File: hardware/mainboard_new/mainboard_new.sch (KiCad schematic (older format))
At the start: 11 parts, among them M1 LOGIC_LEVEL_CONVERTER, Q1 BS170

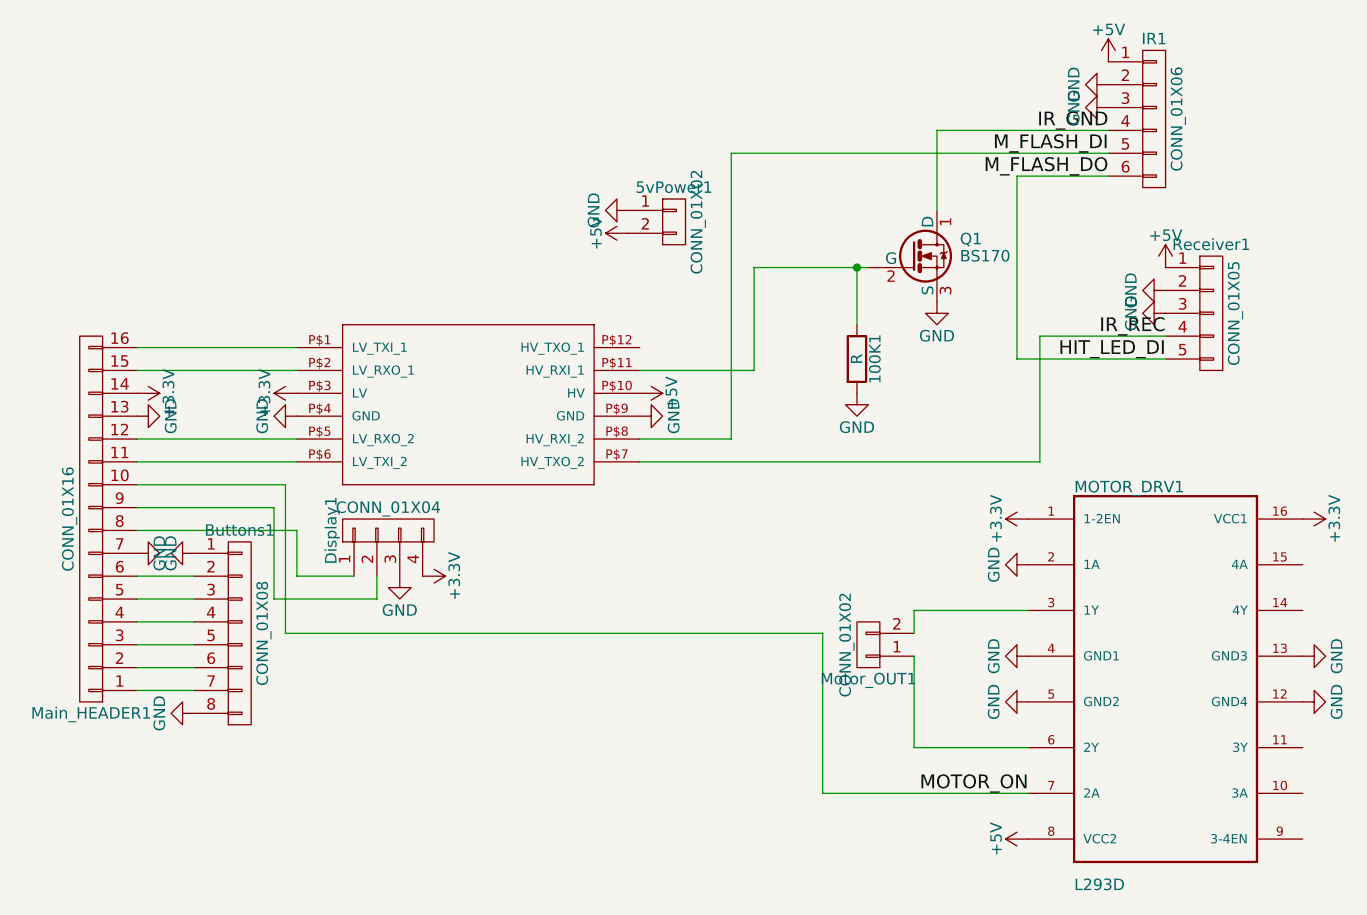
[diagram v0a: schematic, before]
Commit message: #9 JST Pins added
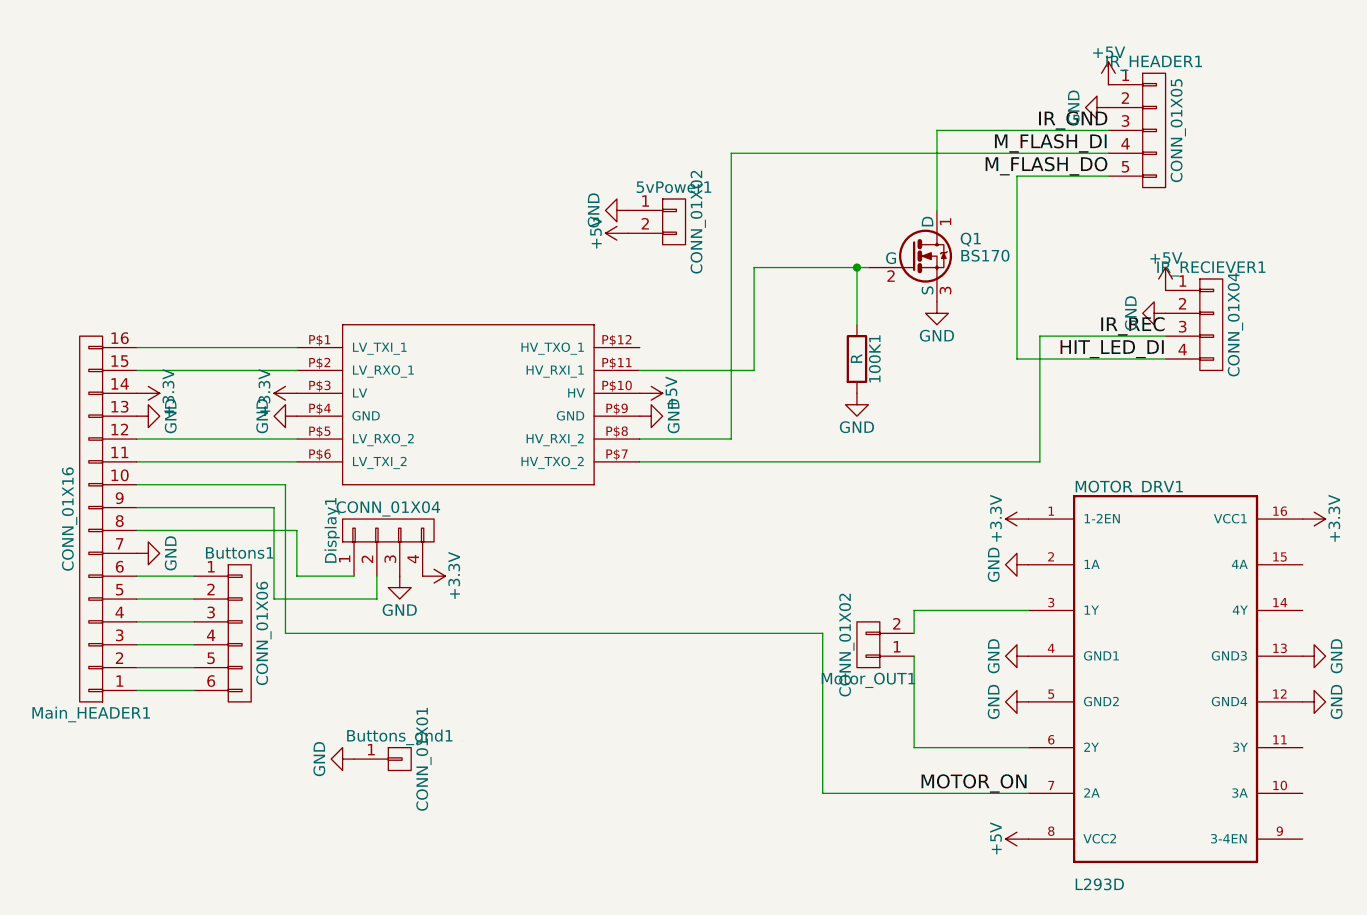
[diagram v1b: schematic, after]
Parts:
- removed Buttons1: CONN_01X08, Socket_Strips:Socket_Strip_Straight_1x08_Pitch2.54mm, symbol CONN_01X08
- removed IR1: CONN_01X06, Socket_Strips:Socket_Strip_Straight_1x06_Pitch2.54mm, symbol CONN_01X06
- removed Receiver1: CONN_01X05, Socket_Strips:Socket_Strip_Straight_1x05_Pitch2.54mm, symbol CONN_01X05
- added Buttons1: CONN_01X06, Connectors_JST:JST_EH_B06B-EH-A_06x2.50mm_Straight, symbol CONN_01X06
- added Buttons_gnd1: CONN_01X01, Socket_Strips:Socket_Strip_Straight_1x01_Pitch1.27mm, symbol CONN_01X01
- added IR_HEADER1: CONN_01X05, Connectors_JST:JST_EH_B05B-EH-A_05x2.50mm_Straight, symbol CONN_01X05
- added IR_RECIEVER1: CONN_01X04, Connectors_JST:JST_EH_B04B-EH-A_04x2.50mm_Straight, symbol CONN_01X04
- 5vPower1: footprint Socket_Strips:Socket_Strip_Straight_1x02_Pitch2.54mm -> Connectors_JST:JST_EH_B02B-EH-A_02x2.50mm_Straight
- Display1: footprint Socket_Strips:Socket_Strip_Straight_1x04_Pitch2.54mm -> Connectors_JST:JST_EH_B04B-EH-A_04x2.50mm_Straight
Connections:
- net +5V: now also IR_HEADER1.1 (P1), IR_RECIEVER1.1 (P1)
- net GND: now also Buttons_gnd1.1 (P1), IR_HEADER1.2 (P2), IR_RECIEVER1.2 (P2)
- net HIT_LED_DI: now also IR_HEADER1.5 (P5), IR_RECIEVER1.4 (P4)
- net IR_GND: now also IR_HEADER1.3 (P3)
- net IR_REC: now also IR_RECIEVER1.3 (P3)
- net M_FLASH_DI: now also IR_HEADER1.4 (P4)
- net at Main_HEADER1.1 (P1): now also Buttons1.6 (P6)
- net at Main_HEADER1.2 (P2): now also Buttons1.5 (P5)
- net at Main_HEADER1.3 (P3): now also Buttons1.4 (P4)
- net at Main_HEADER1.4 (P4): now also Buttons1.3 (P3)
- net at Main_HEADER1.5 (P5): now also Buttons1.2 (P2)
- net at Main_HEADER1.6 (P6): now also Buttons1.1 (P1)
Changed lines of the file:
@@
 F 0 "Display1" H 3300 3800 50  0000 C CNN
 F 1 "CONN_01X04" V 3400 3550 50  0000 C CNN
-F 2 "Socket_Strips:Socket_Strip_Straight_1x04_Pitch2.54mm" H 3300 3550 50  0001 C CNN
+F 2 "Connectors_JST:JST_EH_B04B-EH-A_04x2.50mm_Straight" H 3300 3550 50  0001 C CNN
 F 3 "" H 3300 3550 50  0001 C CNN
 	1    3300 3550
@@
 F 0 "5vPower1" H 4550 2350 50  0000 C CNN
 F 1 "CONN_01X02" V 4650 2200 50  0000 C CNN
-F 2 "Socket_Strips:Socket_Strip_Straight_1x02_Pitch2.54mm" H 4550 2200 50  0001 C CNN
+F 2 "Connectors_JST:JST_EH_B02B-EH-A_02x2.50mm_Straight" H 4550 2200 50  0001 C CNN
 F 3 "" H 4550 2200 50  0001 C CNN
 	1    4550 2200
@@
 $EndComp
 $Comp
-L GND #PWR018
-U 1 1 59666C99
-P 2450 4350
-F 0 "#PWR018" H 2450 4100 50  0001 C CNN
-F 1 "GND" H 2450 4200 50  0000 C CNN
-F 2 "" H 2450 4350 50  0001 C CNN
-F 3 "" H 2450 4350 50  0001 C CNN
-	1    2450 4350
-	0    1    1    0
-$EndComp
-$Comp
-L CONN_01X05 Receiver1
-U 1 1 59666DC7
-P 6900 2600
-F 0 "Receiver1" H 6900 2900 50  0000 C CNN
-F 1 "CONN_01X05" V 7000 2600 50  0000 C CNN
-F 2 "Socket_Strips:Socket_Strip_Straight_1x05_Pitch2.54mm" H 6900 2600 50  0001 C CNN
-F 3 "" H 6900 2600 50  0001 C CNN
-	1    6900 2600
-	1    0    0    -1
-$EndComp
-$Comp
-L +5V #PWR019
+L +5V #PWR017
 U 1 1 59666EE0
-P 6700 2400
-F 0 "#PWR019" H 6700 2250 50  0001 C CNN
-F 1 "+5V" H 6700 2540 50  0000 C CNN
-F 2 "" H 6700 2400 50  0001 C CNN
-F 3 "" H 6700 2400 50  0001 C CNN
-	1    6700 2400
-	1    0    0    -1
-$EndComp
-$Comp
-L GND #PWR020
-U 1 1 59666F02
 P 6700 2500
-F 0 "#PWR020" H 6700 2250 50  0001 C CNN
-F 1 "GND" H 6700 2350 50  0000 C CNN
+F 0 "#PWR017" H 6700 2350 50  0001 C CNN
+F 1 "+5V" H 6700 2640 50  0000 C CNN
 F 2 "" H 6700 2500 50  0001 C CNN
 F 3 "" H 6700 2500 50  0001 C CNN
 	1    6700 2500
-	0    1    1    0
-$EndComp
-$Comp
-L GND #PWR021
+	1    0    0    -1
+$EndComp
+$Comp
+L GND #PWR018
 U 1 1 59666F24
 P 6700 2600
-F 0 "#PWR021" H 6700 2350 50  0001 C CNN
+F 0 "#PWR018" H 6700 2350 50  0001 C CNN
 F 1 "GND" H 6700 2450 50  0000 C CNN
 F 2 "" H 6700 2600 50  0001 C CNN
@@
 $EndComp
 $Comp
-L CONN_01X06 IR1
-U 1 1 59667064
-P 6650 1750
-F 0 "IR1" H 6650 2100 50  0000 C CNN
-F 1 "CONN_01X06" V 6750 1750 50  0000 C CNN
-F 2 "Socket_Strips:Socket_Strip_Straight_1x06_Pitch2.54mm" H 6650 1750 50  0001 C CNN
-F 3 "" H 6650 1750 50  0001 C CNN
-	1    6650 1750
-	1    0    0    -1
-$EndComp
-$Comp
-L +5V #PWR022
+L +5V #PWR019
 U 1 1 596670F4
-P 6450 1500
-F 0 "#PWR022" H 6450 1350 50  0001 C CNN
-F 1 "+5V" H 6450 1640 50  0000 C CNN
-F 2 "" H 6450 1500 50  0001 C CNN
-F 3 "" H 6450 1500 50  0001 C CNN
-	1    6450 1500
-	1    0    0    -1
-$EndComp
-$Comp
-L GND #PWR023
-U 1 1 59667118
 P 6450 1600
-F 0 "#PWR023" H 6450 1350 50  0001 C CNN
-F 1 "GND" H 6450 1450 50  0000 C CNN
+F 0 "#PWR019" H 6450 1450 50  0001 C CNN
+F 1 "+5V" H 6450 1740 50  0000 C CNN
 F 2 "" H 6450 1600 50  0001 C CNN
 F 3 "" H 6450 1600 50  0001 C CNN
 	1    6450 1600
-	0    1    1    0
-$EndComp
-$Comp
-L GND #PWR024
+	1    0    0    -1
+$EndComp
+$Comp
+L GND #PWR020
 U 1 1 5966713C
 P 6450 1700
-F 0 "#PWR024" H 6450 1450 50  0001 C CNN
+F 0 "#PWR020" H 6450 1450 50  0001 C CNN
 F 1 "GND" H 6450 1550 50  0000 C CNN
 F 2 "" H 6450 1700 50  0001 C CNN
@@
 $EndComp
 $Comp
-L GND #PWR025
+L GND #PWR021
 U 1 1 59667252
 P 5350 2950
-F 0 "#PWR025" H 5350 2700 50  0001 C CNN
+F 0 "#PWR021" H 5350 2700 50  0001 C CNN
 F 1 "GND" H 5350 2800 50  0000 C CNN
 F 2 "" H 5350 2950 50  0001 C CNN
@@
 $EndComp
 $Comp
-L GND #PWR026
+L GND #PWR022
 U 1 1 5966727A
 P 5700 2550
-F 0 "#PWR026" H 5700 2300 50  0001 C CNN
+F 0 "#PWR022" H 5700 2300 50  0001 C CNN
 F 1 "GND" H 5700 2400 50  0000 C CNN
 F 2 "" H 5700 2550 50  0001 C CNN
@@
 	2800 3850 3250 3850
 $Comp
-L GND #PWR027
+L GND #PWR023
 U 1 1 59669886
 P 3350 3750
-F 0 "#PWR027" H 3350 3500 50  0001 C CNN
+F 0 "#PWR023" H 3350 3500 50  0001 C CNN
 F 1 "GND" H 3350 3600 50  0000 C CNN
 F 2 "" H 3350 3750 50  0001 C CNN
@@
 $EndComp
 $Comp
-L +3.3V #PWR028
+L +3.3V #PWR024
 U 1 1 596698AE
 P 3450 3750
-F 0 "#PWR028" H 3450 3600 50  0001 C CNN
+F 0 "#PWR024" H 3450 3600 50  0001 C CNN
 F 1 "+3.3V" H 3450 3890 50  0000 C CNN
 F 2 "" H 3450 3750 50  0001 C CNN
@@
 $EndComp
 $Comp
-L GND #PWR029
+L GND #PWR025
 U 1 1 59669E34
 P 4400 3050
-F 0 "#PWR029" H 4400 2800 50  0001 C CNN
+F 0 "#PWR025" H 4400 2800 50  0001 C CNN
 F 1 "GND" H 4400 2900 50  0000 C CNN
 F 2 "" H 4400 3050 50  0001 C CNN
@@
 Wire Wire Line
 	4900 2850 4900 2400
-$Comp
-L CONN_01X08 Buttons1
-U 1 1 59666B16
+Wire Wire Line
+	2200 3750 2450 3750
+Wire Wire Line
+	2200 3850 2450 3850
+Wire Wire Line
+	2200 3950 2450 3950
+Wire Wire Line
+	2200 4050 2450 4050
+Wire Wire Line
+	2200 4150 2450 4150
+Wire Wire Line
+	2200 4250 2450 4250
+$Comp
+L CONN_01X05 IR_HEADER1
+U 1 1 596A1441
+P 6650 1800
+F 0 "IR_HEADER1" H 6650 2100 50  0000 C CNN
+F 1 "CONN_01X05" V 6750 1800 50  0000 C CNN
+F 2 "Connectors_JST:JST_EH_B05B-EH-A_05x2.50mm_Straight" H 6650 1800 50  0001 C CNN
+F 3 "" H 6650 1800 50  0001 C CNN
+	1    6650 1800
+	1    0    0    -1
+$EndComp
+$Comp
+L CONN_01X04 IR_RECIEVER1
+U 1 1 596A153D
+P 6900 2650
+F 0 "IR_RECIEVER1" H 6900 2900 50  0000 C CNN
+F 1 "CONN_01X04" V 7000 2650 50  0000 C CNN
+F 2 "Connectors_JST:JST_EH_B04B-EH-A_04x2.50mm_Straight" H 6900 2650 50  0001 C CNN
+F 3 "" H 6900 2650 50  0001 C CNN
+	1    6900 2650
+	1    0    0    -1
+$EndComp
+$Comp
+L CONN_01X06 Buttons1
+U 1 1 596A19FD
 P 2650 4000
-F 0 "Buttons1" H 2650 4450 50  0000 C CNN
-F 1 "CONN_01X08" V 2750 4000 50  0000 C CNN
-F 2 "Socket_Strips:Socket_Strip_Straight_1x08_Pitch2.54mm" H 2650 4000 50  0001 C CNN
+F 0 "Buttons1" H 2650 4350 50  0000 C CNN
+F 1 "CONN_01X06" V 2750 4000 50  0000 C CNN
+F 2 "Connectors_JST:JST_EH_B06B-EH-A_06x2.50mm_Straight" H 2650 4000 50  0001 C CNN
 F 3 "" H 2650 4000 50  0001 C CNN
 	1    2650 4000
@@
 $EndComp
 $Comp
-L GND #PWR?
-U 1 1 5966ABE0
-P 2450 3650
-F 0 "#PWR?" H 2450 3400 50  0001 C CNN
-F 1 "GND" H 2450 3500 50  0000 C CNN
-F 2 "" H 2450 3650 50  0001 C CNN
-F 3 "" H 2450 3650 50  0001 C CNN
-	1    2450 3650
-	0    1    1    0
-$EndComp
-Wire Wire Line
-	2200 3750 2450 3750
-Wire Wire Line
-	2200 3850 2450 3850
-Wire Wire Line
-	2200 3950 2450 3950
-Wire Wire Line
-	2200 4050 2450 4050
-Wire Wire Line
-	2200 4150 2450 4150
-Wire Wire Line
-	2200 4250 2450 4250
+L CONN_01X01 Buttons_gnd1
+U 1 1 596A1B61
+P 3350 4550
+F 0 "Buttons_gnd1" H 3350 4650 50  0000 C CNN
+F 1 "CONN_01X01" V 3450 4550 50  0000 C CNN
+F 2 "Socket_Strips:Socket_Strip_Straight_1x01_Pitch1.27mm" H 3350 4550 50  0001 C CNN
+F 3 "" H 3350 4550 50  0001 C CNN
+	1    3350 4550
+	1    0    0    -1
+$EndComp
+$Comp
+L GND #PWR026
+U 1 1 596A1B94
+P 3150 4550
+F 0 "#PWR026" H 3150 4300 50  0001 C CNN
+F 1 "GND" H 3150 4400 50  0000 C CNN
+F 2 "" H 3150 4550 50  0001 C CNN
+F 3 "" H 3150 4550 50  0001 C CNN
+	1    3150 4550
+	0    1    1    0
+$EndComp
 $EndSCHEMATC
